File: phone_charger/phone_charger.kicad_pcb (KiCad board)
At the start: 2 copper layers, 22.6 x 30.8 mm, 19 parts, among them J1 Conn_01x02, J2 UE27AC54100, U1 ADP2302

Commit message: Added silkscreens to charger board
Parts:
- added G***: LOGO, phone_charger:ieee-logo-inv, F.Cu at (92.4, 64.0)
- added G***: LOGO, phone_charger:bac-logo, B.Cu at (104.9, 79.3)

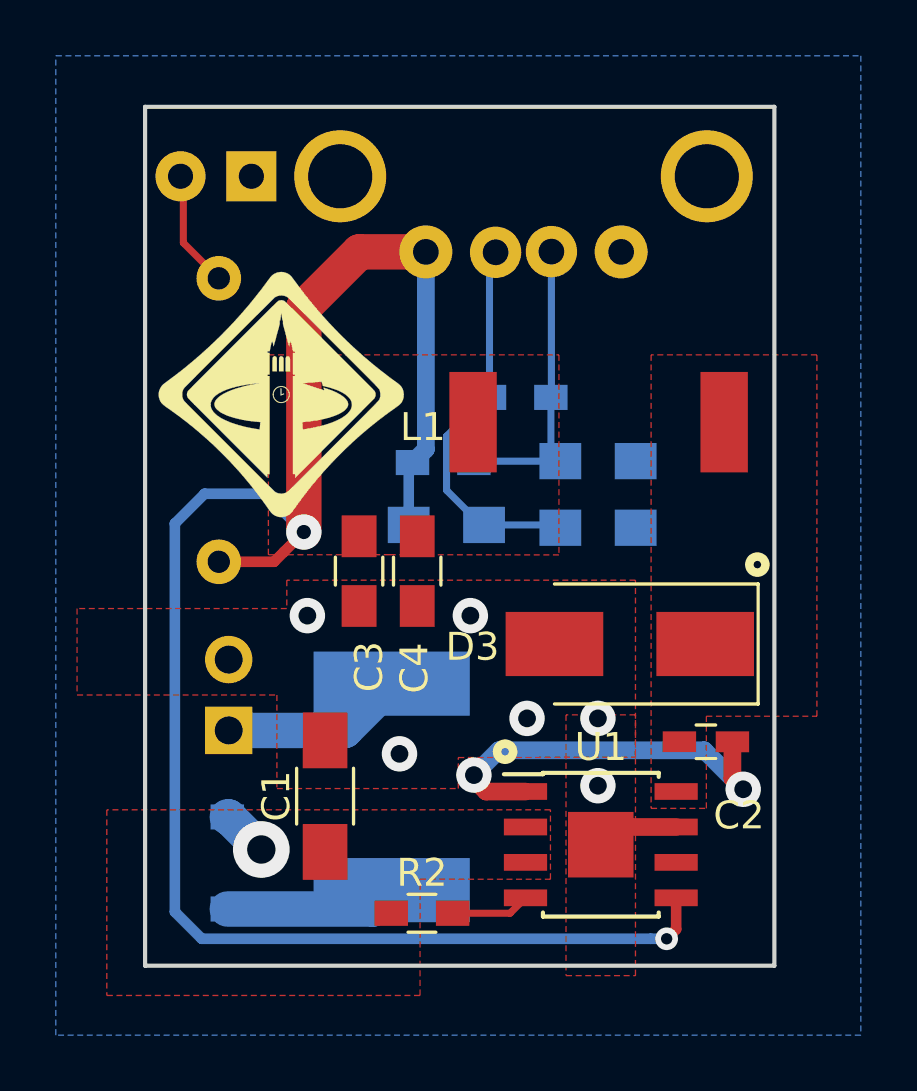
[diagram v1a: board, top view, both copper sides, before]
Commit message: Added fb resistors to phone charger
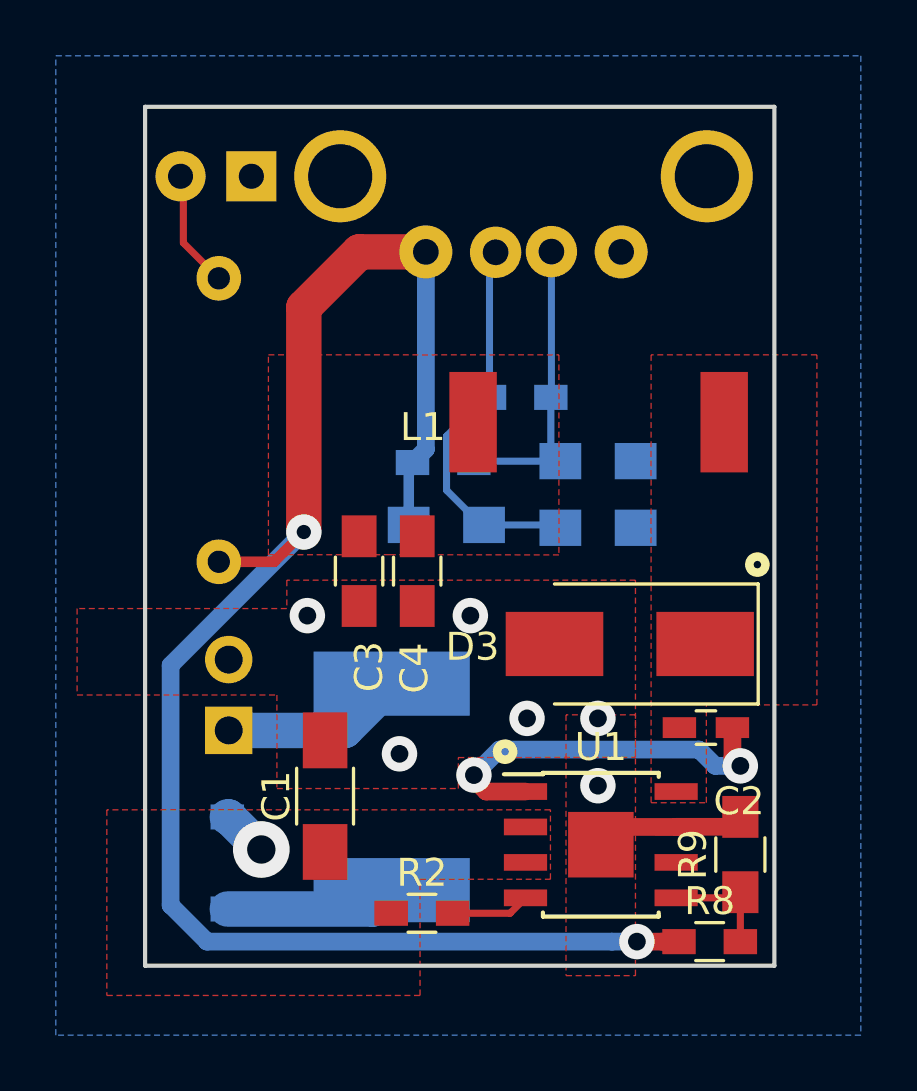
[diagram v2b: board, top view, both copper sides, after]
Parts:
- removed G***: LOGO, phone_charger:ieee-logo-inv
- removed G***: LOGO, phone_charger:bac-logo
- added R8: 52.3k (1%), Resistors_SMD:R_0603_HandSoldering, F.Cu at (107.8, 83.6)
- added R9: 10k (1%), Resistors_SMD:R_0805_HandSoldering, F.Cu at (108.9, 80.4)
- J2: value UE27AC54100 -> SS-52100-001
- moved C2 0.51 mm to (107.6, 75.9)
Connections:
- U1 pad 5: VBUS -> Net-(R8-Pad2)
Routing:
- net VBUS: track 66.0 -> 60.9 mm
- net Net-(R8-Pad2): track 0.00 -> 4.10 mm
- net EPAD: track 6.32 -> 8.78 mm
- net Net-(C2-Pad1): track 14.8 -> 14.0 mm

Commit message: Fixed silkscreen on phone charger circuit
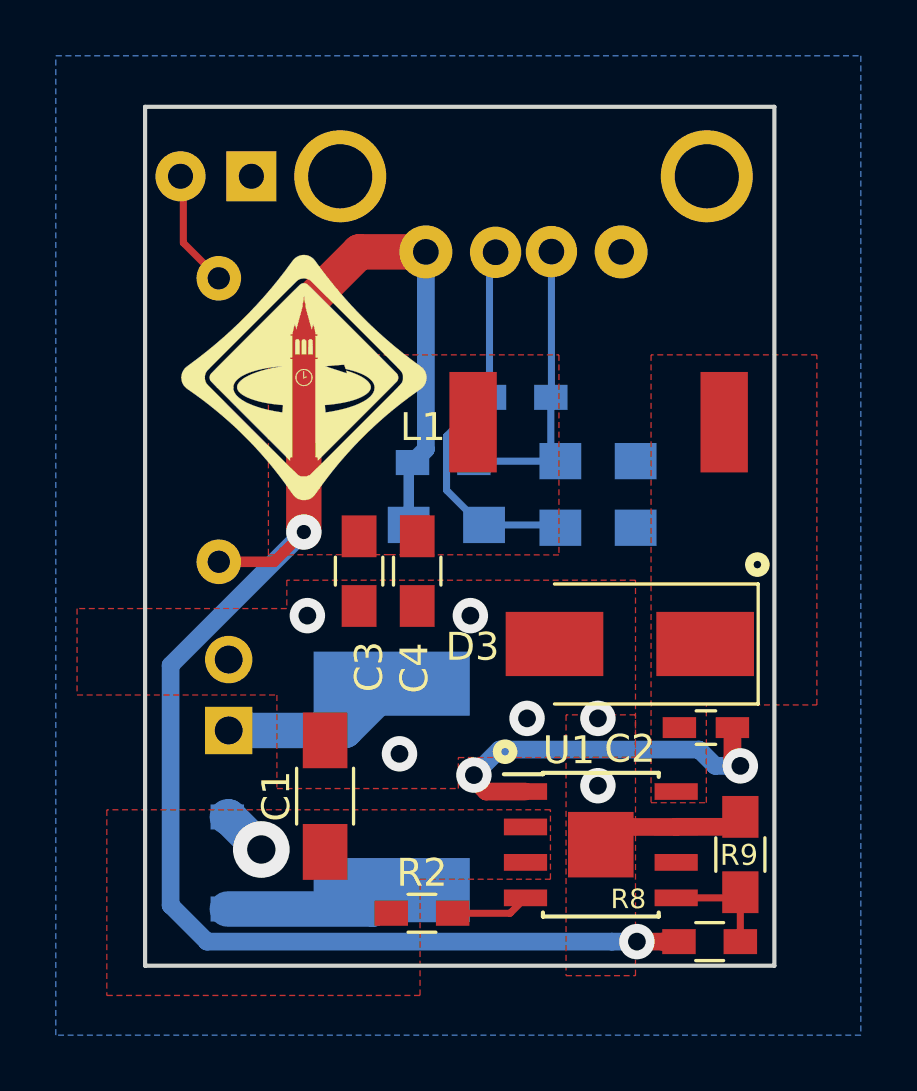
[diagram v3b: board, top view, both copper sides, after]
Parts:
- added G***: LOGO, phone_charger:ieee-logo-inv, F.Cu at (93.2, 63.3)
- added G***: LOGO, phone_charger:bac-logo, B.Cu at (104.2, 79.8)

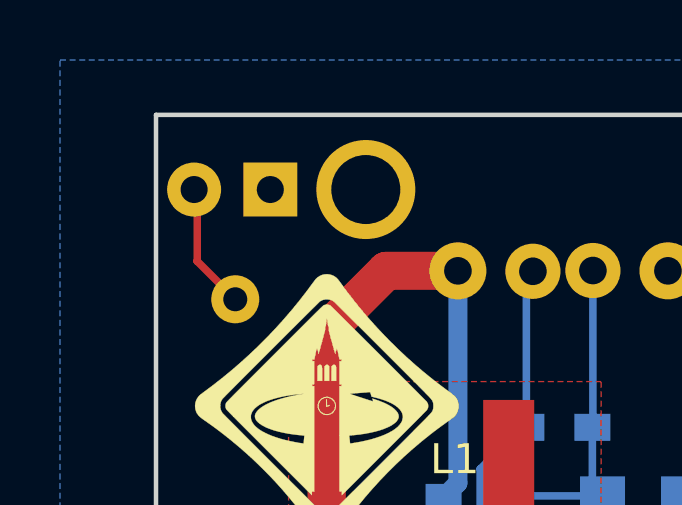
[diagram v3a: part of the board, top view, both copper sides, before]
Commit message: Updated LED hole size phone charger
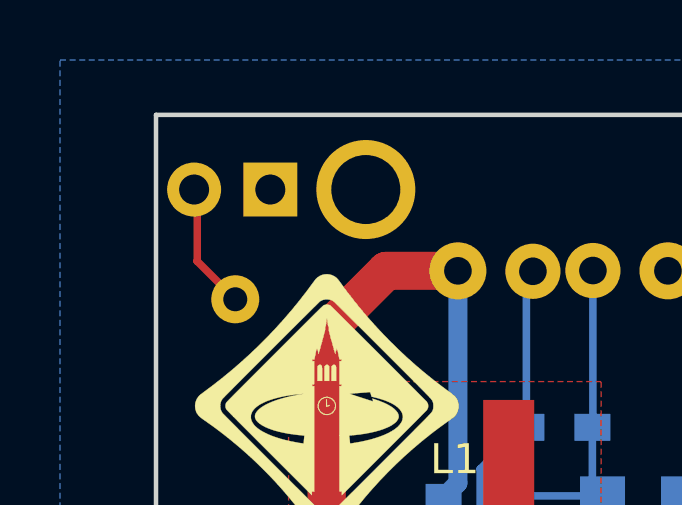
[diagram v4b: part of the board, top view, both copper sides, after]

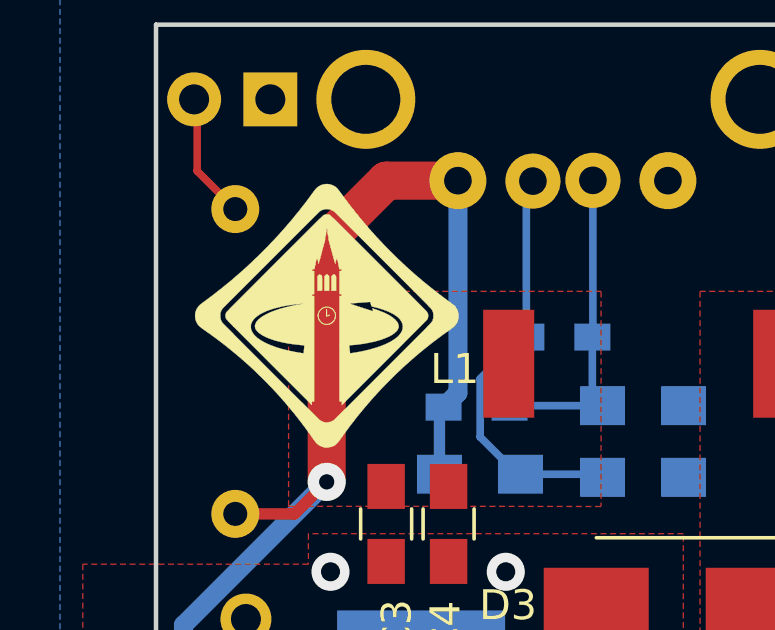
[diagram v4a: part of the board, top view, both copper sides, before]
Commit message: updated schematic with silkscreen logos
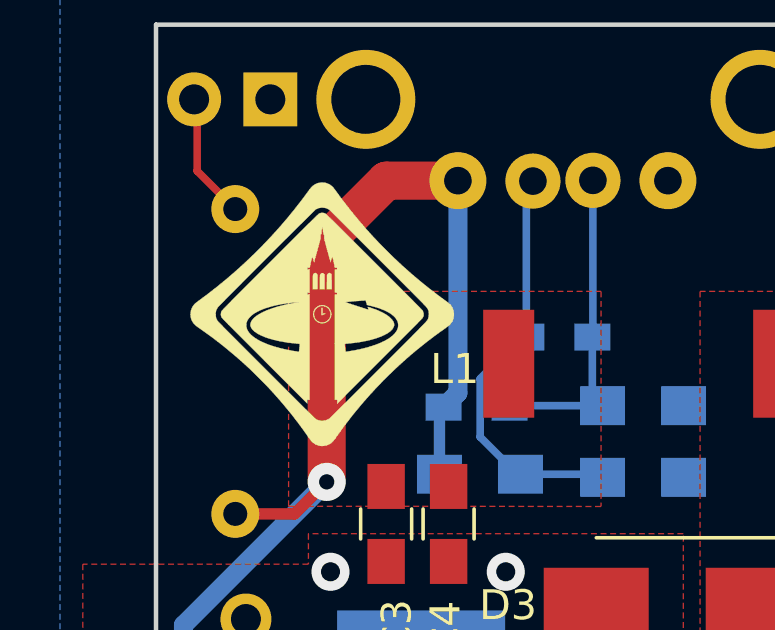
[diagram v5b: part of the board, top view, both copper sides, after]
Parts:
- removed G***: LOGO, phone_charger:ieee-logo-inv
- removed G***: LOGO, phone_charger:bac-logo
- added LOGO1: logo-symbol, phone_charger:bac-logo, B.Cu at (104.9, 79.5)
- added LOGO2: logo-symbol, phone_charger:ieee-logo-inv, F.Cu at (93.1, 63.3)
- D1: footprint LEDs:LED_D3.0mm -> phone_charger:LED_D3.0mm

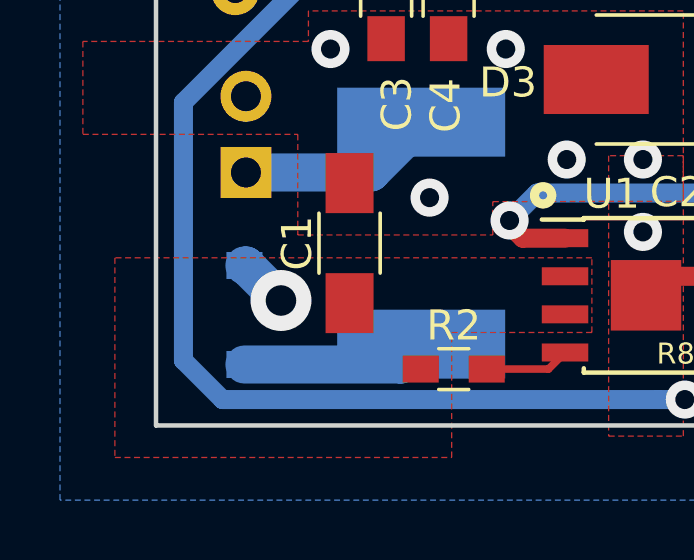
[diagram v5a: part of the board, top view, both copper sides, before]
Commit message: Change diode package to 123H
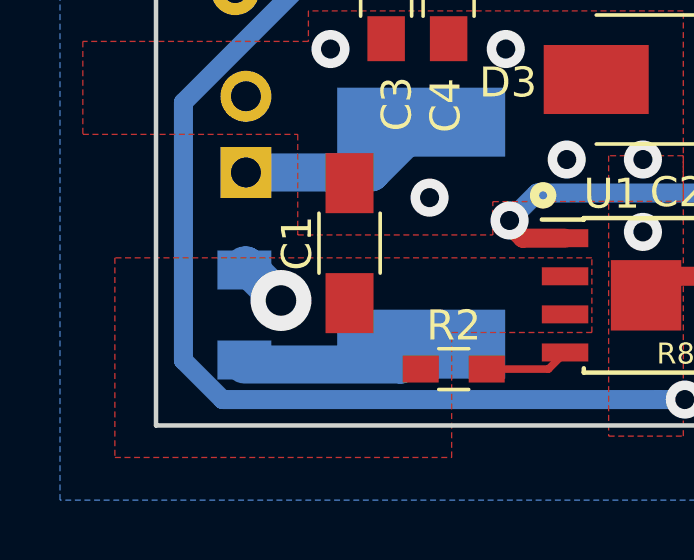
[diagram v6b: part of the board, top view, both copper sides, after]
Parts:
- D2: footprint phone_charger:D_SOD-123 -> Diode_SMD:D_SOD-123H
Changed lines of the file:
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@@
-(kicad_pcb (version 20171130) (host pcbnew "(5.0.0-3-g5ebb6b6)")
+(kicad_pcb (version 20171130) (host pcbnew 6.0.0-rc1-unknown)
   (general
     (thickness 1.5748)
@@
     (zone_45_only no)
     (trace_min 0.1524)
-    (segment_width 0.2)
-    (edge_width 0.15)
     (via_size 0.5588)
     (via_drill 0.254)
@@
     (uvia_min_size 0.2)
     (uvia_min_drill 0.1)
+    (edge_width 0.15)
+    (segment_width 0.2)
     (pcb_text_width 0.3)
     (pcb_text_size 1.5 1.5)
@@
     (uvia_dia 0.5588)
     (uvia_drill 0.254)
+    (diff_pair_width 0.254)
     (diff_pair_gap 0.254)
-    (diff_pair_width 0.254)
     (add_net /D+)
     (add_net /D-)
@@
     (uvia_dia 0.5588)
     (uvia_drill 0.254)
+    (diff_pair_width 0.254)
     (diff_pair_gap 0.254)
-    (diff_pair_width 0.254)
     (add_net /SWN)
     (add_net /reg_in)
@@
     (add_net "Net-(F1-Pad2)")
     (add_net VBUS)
+  )
+  (module Diode_SMD:D_SOD-123H (layer B.Cu)
+    (at 90.4748 80.7476 270)
+    (descr SOD-123)
+    (tags SOD-123)
+    (attr smd)
+    (fp_text reference D2 (at 0 2 270) (layer B.SilkS)
+      (effects (font (size 1 1) (thickness 0.15)) (justify mirror))
+    )
+    (fp_text value D_Schottky (at 0 -2.1 270) (layer B.Fab)
+      (effects (font (size 1 1) (thickness 0.15)) (justify mirror))
+    )
+    (fp_text user %R (at 0 2 270) (layer B.Fab)
+      (effects (font (size 1 1) (thickness 0.15)) (justify mirror))
+    )
+    (fp_line (start -2.25 1) (end -2.25 -1) (layer B.SilkS) (width 0.12))
+    (fp_line (start 0.25 0) (end 0.75 0) (layer B.Fab) (width 0.1))
+    (fp_line (start 0.25 -0.4) (end -0.35 0) (layer B.Fab) (width 0.1))
+    (fp_line (start 0.25 0.4) (end 0.25 -0.4) (layer B.Fab) (width 0.1))
+    (fp_line (start -0.35 0) (end 0.25 0.4) (layer B.Fab) (width 0.1))
+    (fp_line (start -0.35 0) (end -0.35 -0.55) (layer B.Fab) (width 0.1))
+    (fp_line (start -0.35 0) (end -0.35 0.55) (layer B.Fab) (width 0.1))
+    (fp_line (start -0.75 0) (end -0.35 0) (layer B.Fab) (width 0.1))
+    (fp_line (start -1.85 -0.9) (end -1.85 0.9) (layer B.Fab) (width 0.1))
+    (fp_line (start 1.85 0.9) (end 1.85 -0.9) (layer B.Fab) (width 0.1))
+    (fp_line (start -1.85 0.9) (end 1.85 0.9) (layer B.Fab) (width 0.1))
+    (fp_line (start -2.35 1.15) (end 2.35 1.15) (layer B.CrtYd) (width 0.05))
+    (fp_line (start 2.35 1.15) (end 2.35 -1.15) (layer B.CrtYd) (width 0.05))
+    (fp_line (start 2.35 -1.15) (end -2.35 -1.15) (layer B.CrtYd) (width 0.05))
+    (fp_line (start -2.35 1.15) (end -2.35 -1.15) (layer B.CrtYd) (width 0.05))
+    (fp_line (start -2.25 -1) (end 1.65 -1) (layer B.SilkS) (width 0.12))
+    (fp_line (start -2.25 1) (end 1.65 1) (layer B.SilkS) (width 0.12))
+    (fp_line (start -1.85 -0.9) (end 1.85 -0.9) (layer B.Fab) (width 0.1))
+    (pad 1 smd rect (at -1.5 0 270) (size 1.3 1.8) (layers B.Cu B.Paste B.Mask)
+      (net 7 /reg_in))
+    (pad 2 smd rect (at 1.5 0 270) (size 1.3 1.8) (layers B.Cu B.Paste B.Mask)
+      (net 11 "Net-(D2-Pad2)"))
+    (model ${KISYS3DMOD}/Diode_SMD.3dshapes/D_SOD-123.wrl
+      (at (xyz 0 0 0))
+      (scale (xyz 1 1 1))
+      (rotate (xyz 0 0 0))
+    )
   )
   (module phone_charger:LED_D3.0mm (layer B.Cu)
@@
       (at (xyz 0 0 0))
       (scale (xyz 1 1 1))
-      (rotate (xyz 0 0 0))
-    )
-  )
-  (module phone_charger:D_SOD-123 (layer B.Cu)
-    (at 90.4748 80.7476 270)
-    (descr SOD-123)
-    (tags SOD-123)
-    (attr smd)
-    (fp_text reference D2 (at -0.89 1.8796 270) (layer B.SilkS)
-      (effects (font (size 1 1) (thickness 0.15)) (justify mirror))
-    )
-    (fp_text value D_Schottky (at 0 -2.1 270) (layer B.Fab)
-      (effects (font (size 1 1) (thickness 0.15)) (justify mirror))
-    )
-    (fp_text user %R (at 0 2 270) (layer B.Fab)
-      (effects (font (size 1 1) (thickness 0.15)) (justify mirror))
-    )
-    (fp_line (start -2.25 1) (end -2.25 -1) (layer B.SilkS) (width 0.12))
-    (fp_line (start 0.25 0) (end 0.75 0) (layer B.Fab) (width 0.1))
-    (fp_line (start 0.25 -0.4) (end -0.35 0) (layer B.Fab) (width 0.1))
-    (fp_line (start 0.25 0.4) (end 0.25 -0.4) (layer B.Fab) (width 0.1))
-    (fp_line (start -0.35 0) (end 0.25 0.4) (layer B.Fab) (width 0.1))
-    (fp_line (start -0.35 0) (end -0.35 -0.55) (layer B.Fab) (width 0.1))
-    (fp_line (start -0.35 0) (end -0.35 0.55) (layer B.Fab) (width 0.1))
-    (fp_line (start -0.75 0) (end -0.35 0) (layer B.Fab) (width 0.1))
-    (fp_line (start -1.4 -0.9) (end -1.4 0.9) (layer B.Fab) (width 0.1))
-    (fp_line (start 1.4 -0.9) (end -1.4 -0.9) (layer B.Fab) (width 0.1))
-    (fp_line (start 1.4 0.9) (end 1.4 -0.9) (layer B.Fab) (width 0.1))
-    (fp_line (start -1.4 0.9) (end 1.4 0.9) (layer B.Fab) (width 0.1))
-    (fp_line (start -2.35 1.15) (end 2.35 1.15) (layer B.CrtYd) (width 0.05))
-    (fp_line (start 2.35 1.15) (end 2.35 -1.15) (layer B.CrtYd) (width 0.05))
-    (fp_line (start 2.35 -1.15) (end -2.35 -1.15) (layer B.CrtYd) (width 0.05))
-    (fp_line (start -2.35 1.15) (end -2.35 -1.15) (layer B.CrtYd) (width 0.05))
-    (fp_line (start -2.25 -1) (end 1.65 -1) (layer B.SilkS) (width 0.12))
-    (fp_line (start -2.25 1) (end 1.65 1) (layer B.SilkS) (width 0.12))
-    (fp_line (start 0.377 0) (end 0.877 0) (layer B.SilkS) (width 0.1))
-    (fp_line (start 0.377 -0.4) (end -0.223 0) (layer B.SilkS) (width 0.1))
-    (fp_line (start 0.377 0.4) (end 0.377 -0.4) (layer B.SilkS) (width 0.1))
-    (fp_line (start -0.223 0) (end 0.377 0.4) (layer B.SilkS) (width 0.1))
-    (fp_line (start -0.223 0) (end -0.223 -0.55) (layer B.SilkS) (width 0.1))
-    (fp_line (start -0.223 0) (end -0.223 0.55) (layer B.SilkS) (width 0.1))
-    (fp_line (start -0.623 0) (end -0.223 0) (layer B.SilkS) (width 0.1))
-    (pad 1 smd rect (at -1.65 0 270) (size 0.9 1.2) (layers B.Cu B.Paste B.Mask)
-      (net 7 /reg_in))
-    (pad 2 smd rect (at 1.65 0 270) (size 0.9 1.2) (layers B.Cu B.Paste B.Mask)
-      (net 11 "Net-(D2-Pad2)"))
-    (model ${KISYS3DMOD}/Diodes_SMD.3dshapes/D_SOD-123.wrl
-      (at (xyz 0 0 0))
-      (scale (xyz 1 1 1))
